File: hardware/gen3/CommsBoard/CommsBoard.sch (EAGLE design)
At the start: 54 parts, among them U1 ATMEGA165PV-8AU

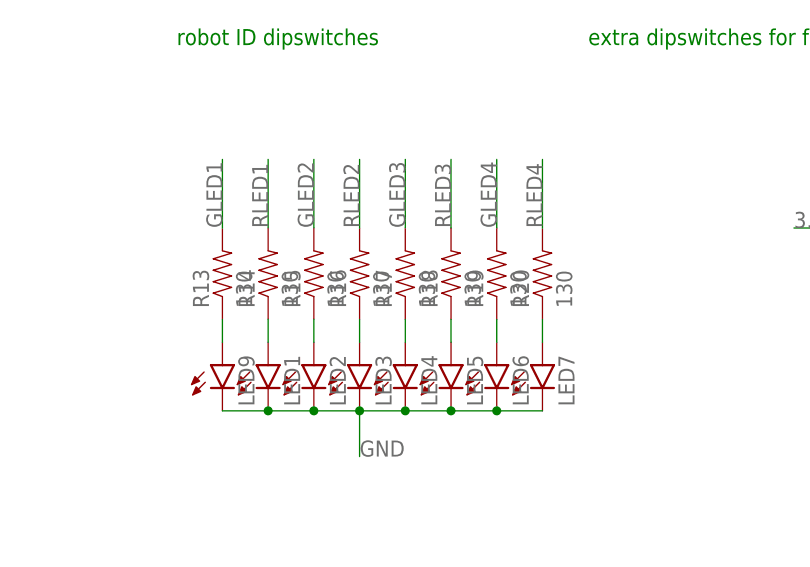
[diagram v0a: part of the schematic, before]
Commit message: resistor values for LEDs
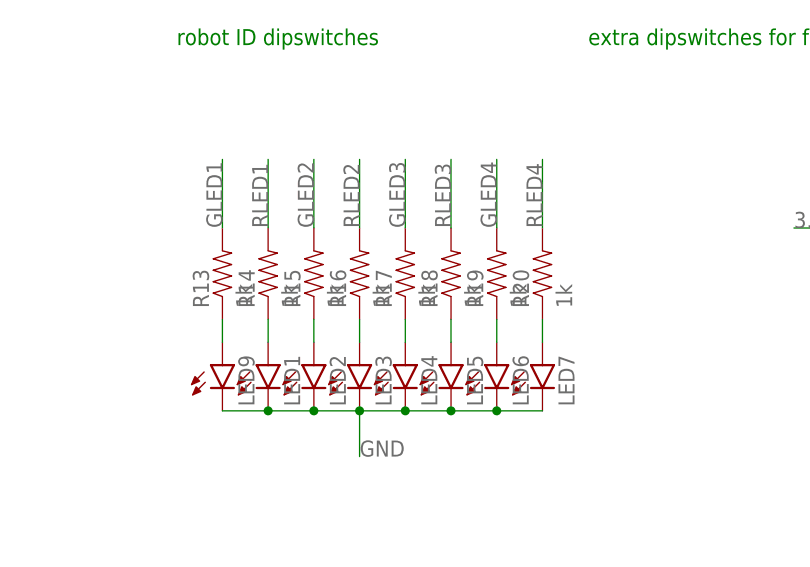
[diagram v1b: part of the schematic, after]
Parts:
- R13, R14, R15, R16, R17, R18, R19, R20: value 130 -> 1k
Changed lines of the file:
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@@
 <part name="R11" library="SparkFun-Passives" deviceset="RESISTOR" device="0805-RES" value="10k"/>
 <part name="R12" library="SparkFun-Passives" deviceset="RESISTOR" device="0805-RES" value="10k"/>
-<part name="R13" library="SparkFun-Passives" deviceset="RESISTOR" device="0805-RES" value="130"/>
-<part name="R14" library="SparkFun-Passives" deviceset="RESISTOR" device="0805-RES" value="130"/>
-<part name="R15" library="SparkFun-Passives" deviceset="RESISTOR" device="0805-RES" value="130"/>
-<part name="R16" library="SparkFun-Passives" deviceset="RESISTOR" device="0805-RES" value="130"/>
-<part name="R17" library="SparkFun-Passives" deviceset="RESISTOR" device="0805-RES" value="130"/>
-<part name="R18" library="SparkFun-Passives" deviceset="RESISTOR" device="0805-RES" value="130"/>
-<part name="R19" library="SparkFun-Passives" deviceset="RESISTOR" device="0805-RES" value="130"/>
-<part name="R20" library="SparkFun-Passives" deviceset="RESISTOR" device="0805-RES" value="130"/>
+<part name="R13" library="SparkFun-Passives" deviceset="RESISTOR" device="0805-RES" value="1k"/>
+<part name="R14" library="SparkFun-Passives" deviceset="RESISTOR" device="0805-RES" value="1k"/>
+<part name="R15" library="SparkFun-Passives" deviceset="RESISTOR" device="0805-RES" value="1k"/>
+<part name="R16" library="SparkFun-Passives" deviceset="RESISTOR" device="0805-RES" value="1k"/>
+<part name="R17" library="SparkFun-Passives" deviceset="RESISTOR" device="0805-RES" value="1k"/>
+<part name="R18" library="SparkFun-Passives" deviceset="RESISTOR" device="0805-RES" value="1k"/>
+<part name="R19" library="SparkFun-Passives" deviceset="RESISTOR" device="0805-RES" value="1k"/>
+<part name="R20" library="SparkFun-Passives" deviceset="RESISTOR" device="0805-RES" value="1k"/>
 <part name="U$1" library="SparkFun-RF" deviceset="XBEE-1" device="B1"/>
 <part name="LED9" library="SparkFun-LED" deviceset="LED" device="1206"/>

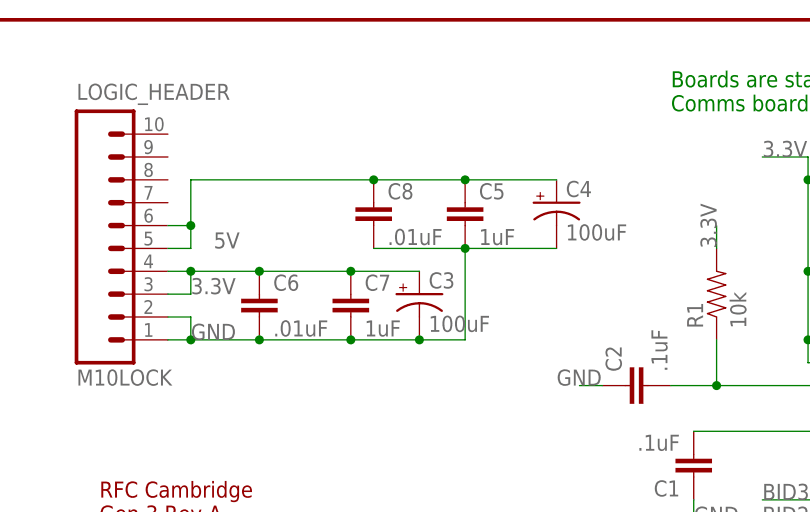
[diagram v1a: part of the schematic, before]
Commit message: using more pins on logic header
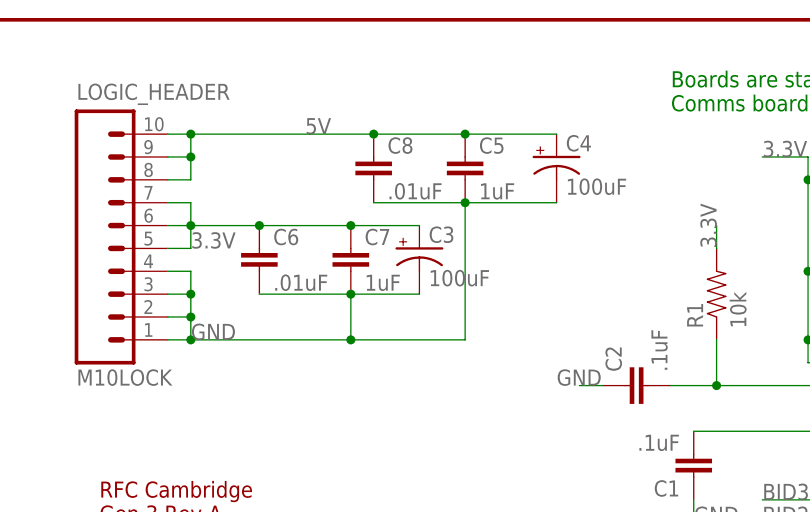
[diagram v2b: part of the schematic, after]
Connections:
- net 3.3V: now also LOGIC_HEADER.5, LOGIC_HEADER.6, LOGIC_HEADER.7; no longer LOGIC_HEADER.3, LOGIC_HEADER.4
- net 5V: now also LOGIC_HEADER.10, LOGIC_HEADER.8, LOGIC_HEADER.9; no longer LOGIC_HEADER.5, LOGIC_HEADER.6
- net GND: now also LOGIC_HEADER.3, LOGIC_HEADER.4
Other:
- moved on the sheet: C3, C4, C5, C6, C7, C8
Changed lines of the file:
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@@
 <instance part="U1" gate="A" x="129.54" y="106.68"/>
 <instance part="JP1" gate="G$1" x="76.2" y="38.1"/>
-<instance part="C5" gate="G$1" x="66.04" y="162.56"/>
-<instance part="C6" gate="G$1" x="43.18" y="152.4"/>
+<instance part="C5" gate="G$1" x="66.04" y="167.64"/>
+<instance part="C6" gate="G$1" x="43.18" y="157.48"/>
 <instance part="U$2" gate="G$1" x="414.02" y="114.3"/>
 <instance part="S1" gate="G$1" x="170.18" y="144.78"/>
 <instance part="R21" gate="G$1" x="172.72" y="132.08"/>
 <instance part="IMU" gate="G$1" x="215.9" y="96.52"/>
-<instance part="C3" gate="G$1" x="60.96" y="154.94"/>
-<instance part="C4" gate="G$1" x="76.2" y="165.1"/>
-<instance part="C7" gate="G$1" x="53.34" y="152.4"/>
-<instance part="C8" gate="G$1" x="55.88" y="162.56"/>
+<instance part="C3" gate="G$1" x="60.96" y="160.02"/>
+<instance part="C4" gate="G$1" x="76.2" y="170.18"/>
+<instance part="C7" gate="G$1" x="53.34" y="157.48"/>
+<instance part="C8" gate="G$1" x="55.88" y="167.64"/>
 <instance part="C9" gate="G$1" x="109.22" y="157.48" rot="R90"/>
 <instance part="C10" gate="G$1" x="109.22" y="167.64" rot="R90"/>
@@
 </segment>
 <segment>
+<pinref part="C4" gate="G$1" pin="-"/>
+<pinref part="C5" gate="G$1" pin="2"/>
+<wire x1="76.2" y1="165.1" x2="66.04" y2="165.1" width="0.1524" layer="91"/>
+<wire x1="66.04" y1="165.1" x2="66.04" y2="149.86" width="0.1524" layer="91"/>
+<junction x="66.04" y="165.1"/>
+<pinref part="C8" gate="G$1" pin="2"/>
+<wire x1="66.04" y1="165.1" x2="55.88" y2="165.1" width="0.1524" layer="91"/>
+<pinref part="LOGIC_HEADER" gate="G$1" pin="1"/>
 <label x="35.56" y="149.86" size="1.778" layer="95"/>
+<wire x1="33.02" y1="149.86" x2="35.56" y2="149.86" width="0.1524" layer="91"/>
 <pinref part="LOGIC_HEADER" gate="G$1" pin="2"/>
+<wire x1="35.56" y1="149.86" x2="53.34" y2="149.86" width="0.1524" layer="91"/>
+<wire x1="53.34" y1="149.86" x2="66.04" y2="149.86" width="0.1524" layer="91"/>
 <wire x1="33.02" y1="152.4" x2="35.56" y2="152.4" width="0.1524" layer="91"/>
 <wire x1="35.56" y1="152.4" x2="35.56" y2="149.86" width="0.1524" layer="91"/>
-<pinref part="LOGIC_HEADER" gate="G$1" pin="1"/>
-<wire x1="35.56" y1="149.86" x2="33.02" y2="149.86" width="0.1524" layer="91"/>
 <junction x="35.56" y="149.86"/>
+<pinref part="LOGIC_HEADER" gate="G$1" pin="3"/>
+<wire x1="33.02" y1="154.94" x2="35.56" y2="154.94" width="0.1524" layer="91"/>
+<wire x1="35.56" y1="154.94" x2="35.56" y2="152.4" width="0.1524" layer="91"/>
+<junction x="35.56" y="152.4"/>
+<pinref part="LOGIC_HEADER" gate="G$1" pin="4"/>
+<wire x1="33.02" y1="157.48" x2="35.56" y2="157.48" width="0.1524" layer="91"/>
+<wire x1="35.56" y1="157.48" x2="35.56" y2="154.94" width="0.1524" layer="91"/>
+<junction x="35.56" y="154.94"/>
 <pinref part="C6" gate="G$1" pin="2"/>
-<wire x1="35.56" y1="149.86" x2="43.18" y2="149.86" width="0.1524" layer="91"/>
-<wire x1="43.18" y1="149.86" x2="53.34" y2="149.86" width="0.1524" layer="91"/>
-<junction x="43.18" y="149.86"/>
+<pinref part="C7" gate="G$1" pin="2"/>
+<wire x1="43.18" y1="154.94" x2="53.34" y2="154.94" width="0.1524" layer="91"/>
 <pinref part="C3" gate="G$1" pin="-"/>
-<pinref part="C4" gate="G$1" pin="-"/>
-<pinref part="C5" gate="G$1" pin="2"/>
-<wire x1="53.34" y1="149.86" x2="60.96" y2="149.86" width="0.1524" layer="91"/>
-<wire x1="76.2" y1="160.02" x2="66.04" y2="160.02" width="0.1524" layer="91"/>
-<wire x1="66.04" y1="160.02" x2="66.04" y2="149.86" width="0.1524" layer="91"/>
-<junction x="66.04" y="160.02"/>
-<wire x1="66.04" y1="149.86" x2="60.96" y2="149.86" width="0.1524" layer="91"/>
-<junction x="60.96" y="149.86"/>
-<pinref part="C7" gate="G$1" pin="2"/>
+<wire x1="53.34" y1="154.94" x2="60.96" y2="154.94" width="0.1524" layer="91"/>
+<junction x="53.34" y="154.94"/>
+<wire x1="53.34" y1="154.94" x2="53.34" y2="149.86" width="0.1524" layer="91"/>
 <junction x="53.34" y="149.86"/>
-<pinref part="C8" gate="G$1" pin="2"/>
-<wire x1="66.04" y1="160.02" x2="55.88" y2="160.02" width="0.1524" layer="91"/>
 </segment>
 <segment>
@@
 </segment>
 <segment>
-<pinref part="LOGIC_HEADER" gate="G$1" pin="3"/>
-<wire x1="33.02" y1="154.94" x2="35.56" y2="154.94" width="0.1524" layer="91"/>
-<label x="35.56" y="154.94" size="1.778" layer="95"/>
-<pinref part="LOGIC_HEADER" gate="G$1" pin="4"/>
-<wire x1="33.02" y1="157.48" x2="35.56" y2="157.48" width="0.1524" layer="91"/>
-<wire x1="35.56" y1="157.48" x2="35.56" y2="154.94" width="0.1524" layer="91"/>
+<label x="35.56" y="160.02" size="1.778" layer="95"/>
 <pinref part="C6" gate="G$1" pin="1"/>
-<wire x1="35.56" y1="157.48" x2="43.18" y2="157.48" width="0.1524" layer="91"/>
-<junction x="35.56" y="157.48"/>
+<wire x1="35.56" y1="162.56" x2="43.18" y2="162.56" width="0.1524" layer="91"/>
 <pinref part="C3" gate="G$1" pin="+"/>
-<wire x1="60.96" y1="157.48" x2="53.34" y2="157.48" width="0.1524" layer="91"/>
-<junction x="43.18" y="157.48"/>
+<wire x1="60.96" y1="162.56" x2="53.34" y2="162.56" width="0.1524" layer="91"/>
+<junction x="43.18" y="162.56"/>
 <pinref part="C7" gate="G$1" pin="1"/>
-<wire x1="53.34" y1="157.48" x2="43.18" y2="157.48" width="0.1524" layer="91"/>
-<junction x="53.34" y="157.48"/>
+<wire x1="53.34" y1="162.56" x2="43.18" y2="162.56" width="0.1524" layer="91"/>
+<junction x="53.34" y="162.56"/>
+<pinref part="LOGIC_HEADER" gate="G$1" pin="5"/>
+<wire x1="33.02" y1="160.02" x2="35.56" y2="160.02" width="0.1524" layer="91"/>
+<wire x1="35.56" y1="160.02" x2="35.56" y2="162.56" width="0.1524" layer="91"/>
+<pinref part="LOGIC_HEADER" gate="G$1" pin="6"/>
+<wire x1="33.02" y1="162.56" x2="35.56" y2="162.56" width="0.1524" layer="91"/>
+<junction x="35.56" y="162.56"/>
+<pinref part="LOGIC_HEADER" gate="G$1" pin="7"/>
+<wire x1="33.02" y1="165.1" x2="35.56" y2="165.1" width="0.1524" layer="91"/>
+<wire x1="35.56" y1="165.1" x2="35.56" y2="162.56" width="0.1524" layer="91"/>
 </segment>
 <segment>
@@
 <net name="5V" class="0">
 <segment>
-<pinref part="LOGIC_HEADER" gate="G$1" pin="5"/>
-<wire x1="33.02" y1="160.02" x2="35.56" y2="160.02" width="0.1524" layer="91"/>
-<label x="38.1" y="160.02" size="1.778" layer="95"/>
-<pinref part="LOGIC_HEADER" gate="G$1" pin="6"/>
-<wire x1="33.02" y1="162.56" x2="35.56" y2="162.56" width="0.1524" layer="91"/>
-<wire x1="35.56" y1="162.56" x2="35.56" y2="160.02" width="0.1524" layer="91"/>
+<label x="48.26" y="172.72" size="1.778" layer="95"/>
 <pinref part="C4" gate="G$1" pin="+"/>
 <pinref part="C5" gate="G$1" pin="1"/>
-<wire x1="76.2" y1="167.64" x2="66.04" y2="167.64" width="0.1524" layer="91"/>
+<wire x1="76.2" y1="172.72" x2="66.04" y2="172.72" width="0.1524" layer="91"/>
 <pinref part="C8" gate="G$1" pin="1"/>
-<wire x1="66.04" y1="167.64" x2="55.88" y2="167.64" width="0.1524" layer="91"/>
-<junction x="66.04" y="167.64"/>
-<wire x1="55.88" y1="167.64" x2="35.56" y2="167.64" width="0.1524" layer="91"/>
-<wire x1="35.56" y1="167.64" x2="35.56" y2="162.56" width="0.1524" layer="91"/>
-<junction x="55.88" y="167.64"/>
-<junction x="35.56" y="162.56"/>
-</segment>
-</net>
+<wire x1="66.04" y1="172.72" x2="55.88" y2="172.72" width="0.1524" layer="91"/>
+<junction x="66.04" y="172.72"/>
+<wire x1="55.88" y1="172.72" x2="35.56" y2="172.72" width="0.1524" layer="91"/>
+<junction x="55.88" y="172.72"/>
+<pinref part="LOGIC_HEADER" gate="G$1" pin="10"/>
+<pinref part="LOGIC_HEADER" gate="G$1" pin="9"/>
+<wire x1="35.56" y1="172.72" x2="33.02" y2="172.72" width="0.1524" layer="91"/>
+<wire x1="33.02" y1="170.18" x2="35.56" y2="170.18" width="0.1524" layer="91"/>
+<wire x1="35.56" y1="170.18" x2="35.56" y2="172.72" width="0.1524" layer="91"/>
+<junction x="35.56" y="172.72"/>
+<pinref part="LOGIC_HEADER" gate="G$1" pin="8"/>
+<wire x1="33.02" y1="167.64" x2="35.56" y2="167.64" width="0.1524" layer="91"/>
+<wire x1="35.56" y1="167.64" x2="35.56" y2="170.18" width="0.1524" layer="91"/>
+<junction x="35.56" y="170.18"/>
+</segment>
+</net>

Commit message: update stuff
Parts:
- renumbered JP1 to PROG, U$1 to XBEE, U$2 to TSENSE
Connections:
- net N$13 renamed PRE-MOSI
- net N$3 renamed PRE-MISO
- net N$4 renamed PRE-SCK
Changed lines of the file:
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@@
 <part name="R19" library="SparkFun-Passives" deviceset="RESISTOR" device="0805-RES" value="1k"/>
 <part name="R20" library="SparkFun-Passives" deviceset="RESISTOR" device="0805-RES" value="1k"/>
-<part name="U$1" library="SparkFun-RF" deviceset="XBEE-1" device="B1"/>
+<part name="XBEE" library="SparkFun-RF" deviceset="XBEE-1" device="B1"/>
 <part name="LED9" library="SparkFun-LED" deviceset="LED" device="1206"/>
 <part name="LED1" library="SparkFun-LED" deviceset="LED" device="1206"/>
@@
 <part name="LED7" library="SparkFun-LED" deviceset="LED" device="1206"/>
 <part name="U1" library="gen3" deviceset="ATMEGA165PV-8AU" device=""/>
-<part name="JP1" library="SparkFun-Connectors" deviceset="M05X2" device="PTH"/>
+<part name="PROG" library="SparkFun-Connectors" deviceset="M05X2" device="PTH"/>
 <part name="C5" library="SparkFun-Capacitors" deviceset="CAP" device="0805" value="1uF"/>
 <part name="C6" library="SparkFun-Capacitors" deviceset="CAP" device="0805" value=".01uF"/>
-<part name="U$2" library="SparkFun-Sensors" deviceset="MCP9700" device="SMD"/>
+<part name="TSENSE" library="SparkFun-Sensors" deviceset="MCP9700" device="SMD"/>
 <part name="S1" library="SparkFun-Electromechanical" deviceset="SWITCH-MOMENTARY-2" device="SMD-4"/>
 <part name="R21" library="SparkFun-Passives" deviceset="RESISTOR" device="0805-RES" value="10k"/>
@@
 <instance part="R19" gate="G$1" x="365.76" y="111.76" rot="R90"/>
 <instance part="R20" gate="G$1" x="370.84" y="111.76" rot="R90"/>
-<instance part="U$1" gate="G$1" x="353.06" y="60.96"/>
+<instance part="XBEE" gate="G$1" x="353.06" y="60.96"/>
 <instance part="LED9" gate="G$1" x="335.28" y="101.6"/>
 <instance part="LED1" gate="G$1" x="340.36" y="101.6"/>
@@
 <instance part="LED7" gate="G$1" x="370.84" y="101.6"/>
 <instance part="U1" gate="A" x="129.54" y="106.68"/>
-<instance part="JP1" gate="G$1" x="76.2" y="38.1"/>
+<instance part="PROG" gate="G$1" x="76.2" y="38.1"/>
 <instance part="C5" gate="G$1" x="66.04" y="167.64"/>
 <instance part="C6" gate="G$1" x="43.18" y="157.48"/>
-<instance part="U$2" gate="G$1" x="414.02" y="114.3"/>
+<instance part="TSENSE" gate="G$1" x="414.02" y="114.3"/>
 <instance part="S1" gate="G$1" x="170.18" y="144.78"/>
 <instance part="R21" gate="G$1" x="172.72" y="132.08"/>
@@
 </segment>
 <segment>
-<pinref part="U$1" gate="G$1" pin="GND"/>
+<pinref part="XBEE" gate="G$1" pin="GND"/>
 <wire x1="332.74" y1="48.26" x2="327.66" y2="48.26" width="0.1524" layer="91"/>
 <label x="327.66" y="48.26" size="1.778" layer="95"/>
@@
 </segment>
 <segment>
-<pinref part="JP1" gate="G$1" pin="10"/>
+<pinref part="PROG" gate="G$1" pin="10"/>
 <wire x1="83.82" y1="33.02" x2="86.36" y2="33.02" width="0.1524" layer="91"/>
-<pinref part="JP1" gate="G$1" pin="8"/>
+<pinref part="PROG" gate="G$1" pin="8"/>
 <wire x1="86.36" y1="33.02" x2="88.9" y2="33.02" width="0.1524" layer="91"/>
 <wire x1="83.82" y1="35.56" x2="86.36" y2="35.56" width="0.1524" layer="91"/>
 <wire x1="86.36" y1="35.56" x2="86.36" y2="33.02" width="0.1524" layer="91"/>
 <junction x="86.36" y="33.02"/>
-<pinref part="JP1" gate="G$1" pin="6"/>
+<pinref part="PROG" gate="G$1" pin="6"/>
 <wire x1="83.82" y1="38.1" x2="86.36" y2="38.1" width="0.1524" layer="91"/>
 <wire x1="86.36" y1="38.1" x2="86.36" y2="35.56" width="0.1524" layer="91"/>
 <junction x="86.36" y="35.56"/>
-<pinref part="JP1" gate="G$1" pin="4"/>
+<pinref part="PROG" gate="G$1" pin="4"/>
 <wire x1="83.82" y1="40.64" x2="86.36" y2="40.64" width="0.1524" layer="91"/>
 <wire x1="86.36" y1="40.64" x2="86.36" y2="38.1" width="0.1524" layer="91"/>
@@
 </segment>
 <segment>
-<pinref part="U$2" gate="G$1" pin="GND"/>
+<pinref part="TSENSE" gate="G$1" pin="GND"/>
 <wire x1="414.02" y1="109.22" x2="414.02" y2="104.14" width="0.1524" layer="91"/>
 <label x="414.02" y="104.14" size="1.778" layer="95"/>
@@
 </segment>
 <segment>
-<pinref part="U$1" gate="G$1" pin="VDD"/>
+<pinref part="XBEE" gate="G$1" pin="VDD"/>
 <wire x1="332.74" y1="71.12" x2="327.66" y2="71.12" width="0.1524" layer="91"/>
 <label x="327.66" y="71.12" size="1.778" layer="95"/>
@@
 </segment>
 <segment>
-<pinref part="JP1" gate="G$1" pin="2"/>
+<pinref part="PROG" gate="G$1" pin="2"/>
 <wire x1="83.82" y1="43.18" x2="88.9" y2="43.18" width="0.1524" layer="91"/>
 <label x="86.36" y="43.18" size="1.778" layer="95"/>
 </segment>
 <segment>
-<pinref part="U$2" gate="G$1" pin="VCC"/>
+<pinref part="TSENSE" gate="G$1" pin="VCC"/>
 <wire x1="403.86" y1="116.84" x2="398.78" y2="116.84" width="0.1524" layer="91"/>
 <label x="398.78" y="116.84" size="1.778" layer="95"/>
@@
 </segment>
 <segment>
-<pinref part="JP1" gate="G$1" pin="1"/>
+<pinref part="PROG" gate="G$1" pin="1"/>
 <wire x1="68.58" y1="43.18" x2="63.5" y2="43.18" width="0.1524" layer="91"/>
 <label x="60.96" y="43.18" size="1.778" layer="95"/>
@@
 </segment>
 <segment>
-<pinref part="JP1" gate="G$1" pin="9"/>
+<pinref part="PROG" gate="G$1" pin="9"/>
 <wire x1="68.58" y1="33.02" x2="63.5" y2="33.02" width="0.1524" layer="91"/>
 <label x="60.96" y="33.02" size="1.778" layer="95"/>
@@
 </segment>
 <segment>
-<pinref part="JP1" gate="G$1" pin="7"/>
+<pinref part="PROG" gate="G$1" pin="7"/>
 <wire x1="68.58" y1="35.56" x2="63.5" y2="35.56" width="0.1524" layer="91"/>
 <label x="60.96" y="35.56" size="1.778" layer="95"/>
@@
 </segment>
 </net>
-<net name="N$3" class="0">
+<net name="PRE-MISO" class="0">
 <segment>
 <pinref part="SPI_HEADER" gate="G$1" pin="2"/>
@@
 </segment>
 </net>
-<net name="N$4" class="0">
+<net name="PRE-SCK" class="0">
 <segment>
 <pinref part="SPI_HEADER" gate="G$1" pin="3"/>
@@
 </segment>
 <segment>
-<pinref part="JP1" gate="G$1" pin="5"/>
+<pinref part="PROG" gate="G$1" pin="5"/>
 <wire x1="68.58" y1="38.1" x2="63.5" y2="38.1" width="0.1524" layer="91"/>
 <label x="60.96" y="38.1" size="1.778" layer="95"/>
@@
 <net name="RX" class="0">
 <segment>
-<pinref part="U$1" gate="G$1" pin="DOUT"/>
+<pinref part="XBEE" gate="G$1" pin="DOUT"/>
 <wire x1="332.74" y1="68.58" x2="327.66" y2="68.58" width="0.1524" layer="91"/>
 <label x="327.66" y="68.58" size="1.778" layer="95"/>
@@
 <net name="TX" class="0">
 <segment>
-<pinref part="U$1" gate="G$1" pin="DIN"/>
+<pinref part="XBEE" gate="G$1" pin="DIN"/>
 <wire x1="332.74" y1="66.04" x2="327.66" y2="66.04" width="0.1524" layer="91"/>
 <label x="327.66" y="66.04" size="1.778" layer="95"/>
@@
 </segment>
 </net>
-<net name="N$13" class="0">
+<net name="PRE-MOSI" class="0">
 <segment>
 <pinref part="SPI_HEADER" gate="G$1" pin="1"/>
@@
 <net name="XBRST" class="0">
 <segment>
-<pinref part="U$1" gate="G$1" pin="RESET"/>
+<pinref part="XBEE" gate="G$1" pin="RESET"/>
 <wire x1="332.74" y1="60.96" x2="325.12" y2="60.96" width="0.1524" layer="91"/>
 <label x="325.12" y="60.96" size="1.778" layer="95"/>
@@
 <net name="RTS" class="0">
 <segment>
-<pinref part="U$1" gate="G$1" pin="RTS"/>
+<pinref part="XBEE" gate="G$1" pin="RTS"/>
 <wire x1="373.38" y1="60.96" x2="378.46" y2="60.96" width="0.1524" layer="91"/>
 <label x="375.92" y="60.96" size="1.778" layer="95"/>
@@
 <net name="CTS" class="0">
 <segment>
-<pinref part="U$1" gate="G$1" pin="CTS"/>
+<pinref part="XBEE" gate="G$1" pin="CTS"/>
 <wire x1="373.38" y1="50.8" x2="378.46" y2="50.8" width="0.1524" layer="91"/>
 <label x="375.92" y="50.8" size="1.778" layer="95"/>
@@
 <net name="TSENSE" class="0">
 <segment>
-<pinref part="U$2" gate="G$1" pin="VO"/>
+<pinref part="TSENSE" gate="G$1" pin="VO"/>
 <wire x1="424.18" y1="116.84" x2="429.26" y2="116.84" width="0.1524" layer="91"/>
 <label x="429.26" y="116.84" size="1.778" layer="95"/>
